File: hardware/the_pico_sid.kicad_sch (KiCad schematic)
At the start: 20 parts, among them J2 Conn_01x05, Q1 2N7002, Q2 2N7002, U1 LM324, U2 SID_6581, U3 Pico, U4 4050, U5 4050, U6 74HC245

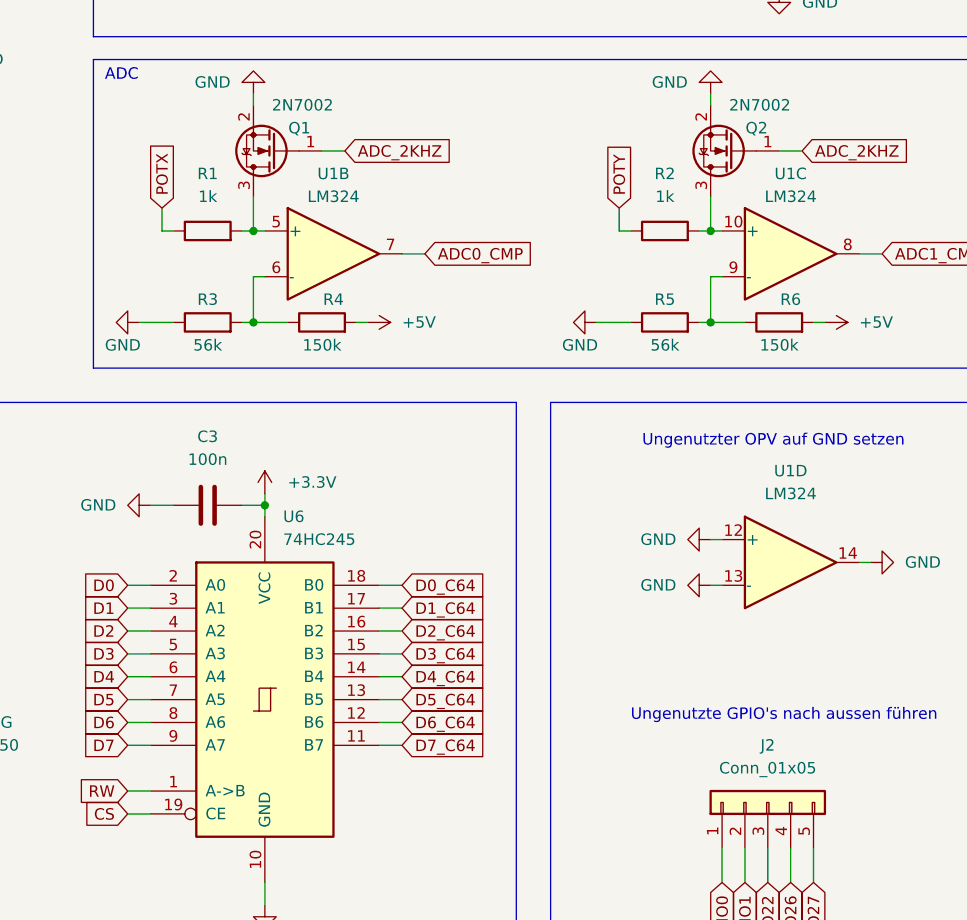
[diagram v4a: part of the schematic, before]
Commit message: change schematic: adc's inverted input voltage from 1.2V to 1.7V
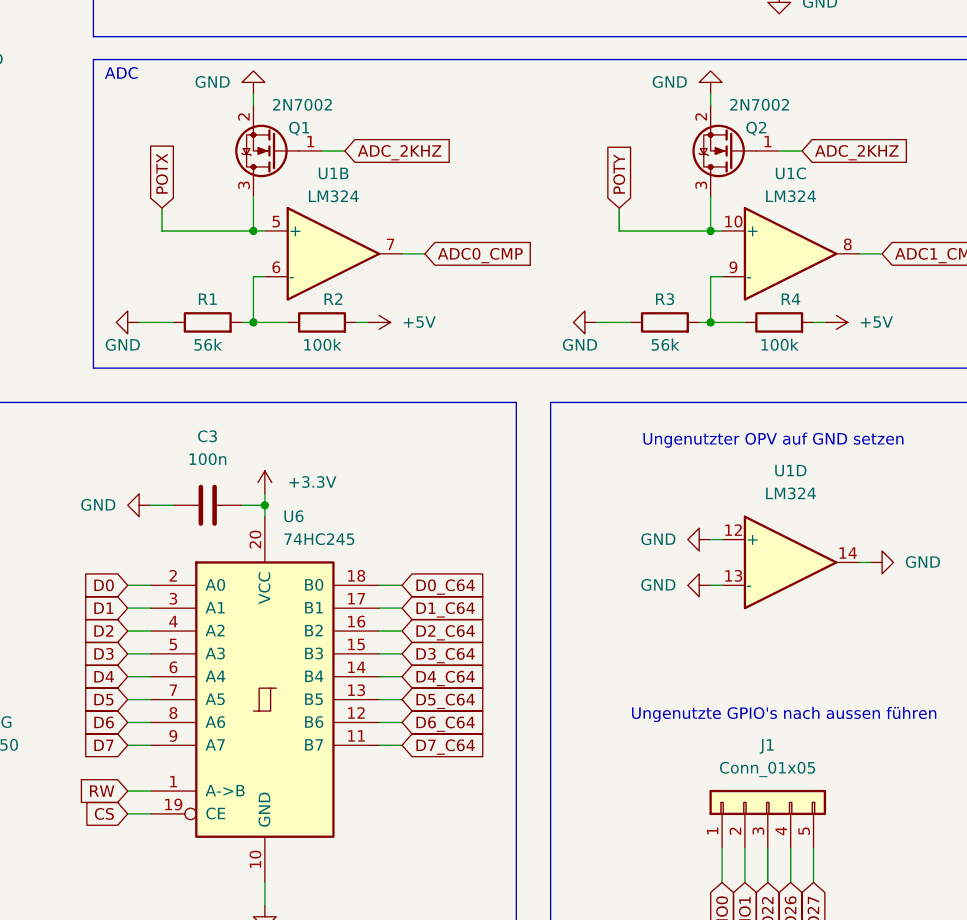
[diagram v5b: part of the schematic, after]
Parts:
- removed R1, R2: 1k, Resistor_SMD:R_0805_2012Metric_Pad1.20x1.40mm_HandSolder, symbol Device:R
- R2: renamed from R4; value 150k -> 100k
- R4: renamed from R6; value 150k -> 100k
- renumbered J2 to J1, R3 to R1, R5 to R3
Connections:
- net POTX: now also Q1.3 (D), U1.5 (+)
- net POTY: now also Q2.3 (D), U1.10 (+)
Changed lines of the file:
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@@
   (title_block
     (title "ThePicoSID")
-    (date "2023-10-09")
-    (rev "1.3")
+    (date "2024-01-25")
+    (rev "1.4")
     (company "Thorsten Kattanek")
   )
@@
     (stroke (width 0) (type default) (color 0 0 0 0))
   )
-  (wire (pts (xy 242.57 74.93) (xy 243.84 74.93))
-    (stroke (width 0) (type default) (color 0 0 0 0))
-  )
   (wire (pts (xy 207.01 121.92) (xy 209.55 121.92))
     (stroke (width 0) (type default) (color 0 0 0 0))
@@
     (stroke (width 0) (type default) (color 0 0 0 0))
   )
-  (wire (pts (xy 233.68 74.93) (xy 234.95 74.93))
+  (wire (pts (xy 233.68 74.93) (xy 243.84 74.93))
     (stroke (width 0) (type default) (color 0 0 0 0))
   )
@@
     (stroke (width 0) (type default) (color 0 0 0 0))
   )
-  (wire (pts (xy 191.77 74.93) (xy 193.04 74.93))
+  (wire (pts (xy 182.88 74.93) (xy 193.04 74.93))
     (stroke (width 0) (type default) (color 0 0 0 0))
   )
@@
   )
   (wire (pts (xy 207.01 124.46) (xy 209.55 124.46))
-    (stroke (width 0) (type default) (color 0 0 0 0))
-  )
-  (wire (pts (xy 182.88 74.93) (xy 184.15 74.93))
     (stroke (width 0) (type default) (color 0 0 0 0))
   )
@@
   (symbol (lib_id "Connector_Generic:Conn_01x05") (at 250.19 138.43 90) (unit 1)
     (in_bom yes) (on_board yes) (fields_autoplaced)
-    (property "Reference" "J2" (id 0) (at 250.19 132.08 90))
+    (property "Reference" "J1" (id 0) (at 250.19 132.08 90))
     (property "Value" "Conn_01x05" (id 1) (at 250.19 134.62 90))
     (property "Footprint" "Connector_PinHeader_2.54mm:PinHeader_1x05_P2.54mm_Vertical" (id 2) (at 250.19 138.43 0)
@@
     )
     (pin "1")
-  )
-  (symbol (lib_id "Device:R") (at 187.96 74.93 90) (unit 1)
-    (in_bom yes) (on_board yes) (fields_autoplaced)
-    (property "Reference" "R1" (id 0) (at 187.96 68.58 90))
-    (property "Value" "1k" (id 1) (at 187.96 71.12 90))
-    (property "Footprint" "Resistor_SMD:R_0805_2012Metric_Pad1.20x1.40mm_HandSolder" (id 2) (at 187.96 76.708 90)
-      (effects (font (size 1.27 1.27)) hide)
-    )
-    (property "Datasheet" "~" (id 3) (at 187.96 74.93 0)
-      (effects (font (size 1.27 1.27)) hide)
-    )
-    (pin "1")
-    (pin "2")
   )
   (symbol (lib_id "Device:C_Polarized") (at 199.39 35.56 90) (unit 1)
@@
   (symbol (lib_id "Device:R") (at 200.66 85.09 90) (unit 1)
     (in_bom yes) (on_board yes)
-    (property "Reference" "R4" (id 0) (at 201.93 82.55 90))
-    (property "Value" "150k" (id 1) (at 200.66 87.63 90))
+    (property "Reference" "R2" (id 0) (at 201.93 82.55 90))
+    (property "Value" "100k" (id 1) (at 200.66 87.63 90))
     (property "Footprint" "Resistor_SMD:R_0805_2012Metric_Pad1.20x1.40mm_HandSolder" (id 2) (at 200.66 86.868 90)
       (effects (font (size 1.27 1.27)) hide)
@@
   (symbol (lib_id "Device:R") (at 251.46 85.09 90) (unit 1)
     (in_bom yes) (on_board yes)
-    (property "Reference" "R6" (id 0) (at 252.73 82.55 90))
-    (property "Value" "150k" (id 1) (at 251.46 87.63 90))
+    (property "Reference" "R4" (id 0) (at 252.73 82.55 90))
+    (property "Value" "100k" (id 1) (at 251.46 87.63 90))
     (property "Footprint" "Resistor_SMD:R_0805_2012Metric_Pad1.20x1.40mm_HandSolder" (id 2) (at 251.46 86.868 90)
       (effects (font (size 1.27 1.27)) hide)
@@
   (symbol (lib_id "Device:R") (at 187.96 85.09 90) (unit 1)
     (in_bom yes) (on_board yes)
-    (property "Reference" "R3" (id 0) (at 187.96 82.55 90))
+    (property "Reference" "R1" (id 0) (at 187.96 82.55 90))
     (property "Value" "56k" (id 1) (at 187.96 87.63 90))
     (property "Footprint" "Resistor_SMD:R_0805_2012Metric_Pad1.20x1.40mm_HandSolder" (id 2) (at 187.96 86.868 90)
@@
     (pin "1")
   )
-  (symbol (lib_id "Device:R") (at 238.76 74.93 90) (unit 1)
-    (in_bom yes) (on_board yes) (fields_autoplaced)
-    (property "Reference" "R2" (id 0) (at 238.76 68.58 90))
-    (property "Value" "1k" (id 1) (at 238.76 71.12 90))
-    (property "Footprint" "Resistor_SMD:R_0805_2012Metric_Pad1.20x1.40mm_HandSolder" (id 2) (at 238.76 76.708 90)
-      (effects (font (size 1.27 1.27)) hide)
-    )
-    (property "Datasheet" "~" (id 3) (at 238.76 74.93 0)
-      (effects (font (size 1.27 1.27)) hide)
-    )
-    (pin "1")
-    (pin "2")
-  )
   (symbol (lib_id "Device:R") (at 238.76 85.09 90) (unit 1)
     (in_bom yes) (on_board yes)
-    (property "Reference" "R5" (id 0) (at 238.76 82.55 90))
+    (property "Reference" "R3" (id 0) (at 238.76 82.55 90))
     (property "Value" "56k" (id 1) (at 238.76 87.63 90))
     (property "Footprint" "Resistor_SMD:R_0805_2012Metric_Pad1.20x1.40mm_HandSolder" (id 2) (at 238.76 86.868 90)
@@
     )
     (path "/0b8132e4-5885-4336-9e9b-cd3d727c8b21"
-      (reference "J2") (unit 1) (value "Conn_01x05") (footprint "Connector_PinHeader_2.54mm:PinHeader_1x05_P2.54mm_Vertical")
+      (reference "J1") (unit 1) (value "Conn_01x05") (footprint "Connector_PinHeader_2.54mm:PinHeader_1x05_P2.54mm_Vertical")
     )
     (path "/e310122b-a6b6-45c4-bf28-e73538f1fd54"
@@
       (reference "Q2") (unit 1) (value "2N7002") (footprint "Package_TO_SOT_SMD:SOT-23")
     )
-    (path "/0f0eabd7-4d8a-45f6-8c35-b26564631504"
-      (reference "R1") (unit 1) (value "1k") (footprint "Resistor_SMD:R_0805_2012Metric_Pad1.20x1.40mm_HandSolder")
-    )
-    (path "/c1e4c0d2-30e7-452a-b9fa-0679cdc25434"
-      (reference "R2") (unit 1) (value "1k") (footprint "Resistor_SMD:R_0805_2012Metric_Pad1.20x1.40mm_HandSolder")
-    )
     (path "/8f635830-c076-4859-8b75-6f7277421c92"
+      (reference "R1") (unit 1) (value "56k") (footprint "Resistor_SMD:R_0805_2012Metric_Pad1.20x1.40mm_HandSolder")
+    )
+    (path "/5b03de6a-f68d-4d73-a978-3777bbbf8fb1"
+      (reference "R2") (unit 1) (value "100k") (footprint "Resistor_SMD:R_0805_2012Metric_Pad1.20x1.40mm_HandSolder")
+    )
+    (path "/c339dda8-004b-4c29-b5ab-577b17fcd28d"
       (reference "R3") (unit 1) (value "56k") (footprint "Resistor_SMD:R_0805_2012Metric_Pad1.20x1.40mm_HandSolder")
     )
-    (path "/5b03de6a-f68d-4d73-a978-3777bbbf8fb1"
-      (reference "R4") (unit 1) (value "150k") (footprint "Resistor_SMD:R_0805_2012Metric_Pad1.20x1.40mm_HandSolder")
-    )
-    (path "/c339dda8-004b-4c29-b5ab-577b17fcd28d"
-      (reference "R5") (unit 1) (value "56k") (footprint "Resistor_SMD:R_0805_2012Metric_Pad1.20x1.40mm_HandSolder")
-    )
     (path "/81649c43-29bd-46d8-b79a-e420ca2ce355"
-      (reference "R6") (unit 1) (value "150k") (footprint "Resistor_SMD:R_0805_2012Metric_Pad1.20x1.40mm_HandSolder")
+      (reference "R4") (unit 1) (value "100k") (footprint "Resistor_SMD:R_0805_2012Metric_Pad1.20x1.40mm_HandSolder")
     )
     (path "/70cd147c-d682-437f-9824-8098d9c94dc4"

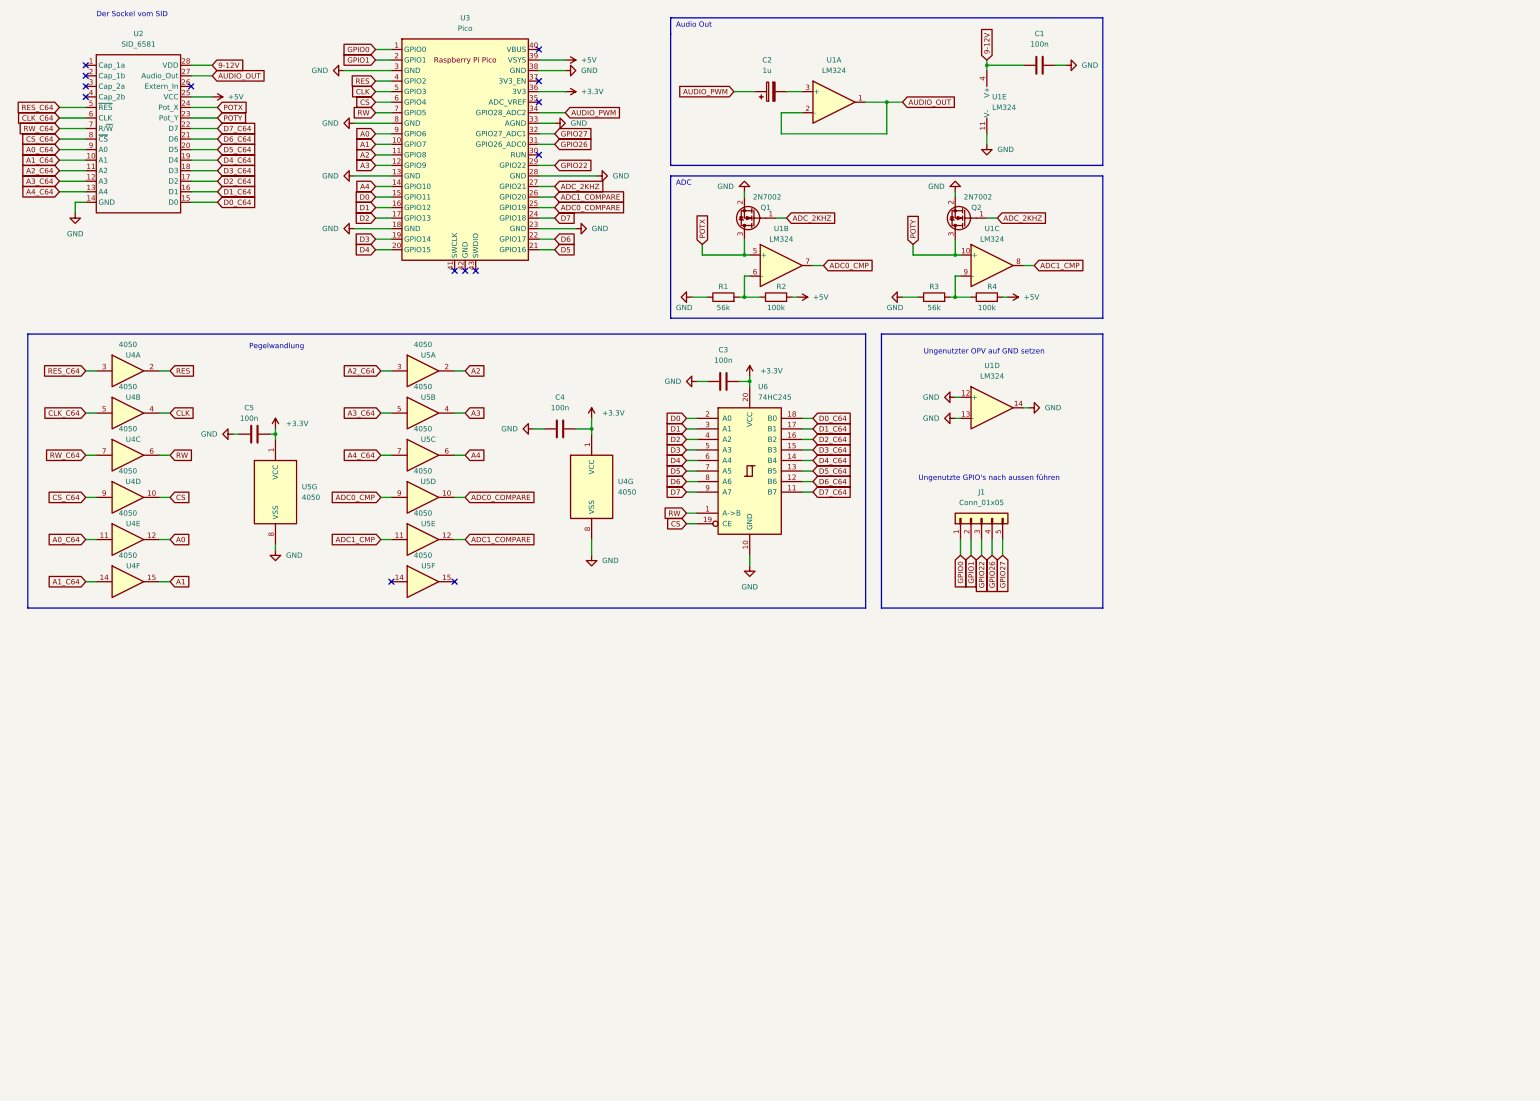
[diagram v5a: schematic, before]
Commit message: schematic: change from 4050 to resistors for level convertion
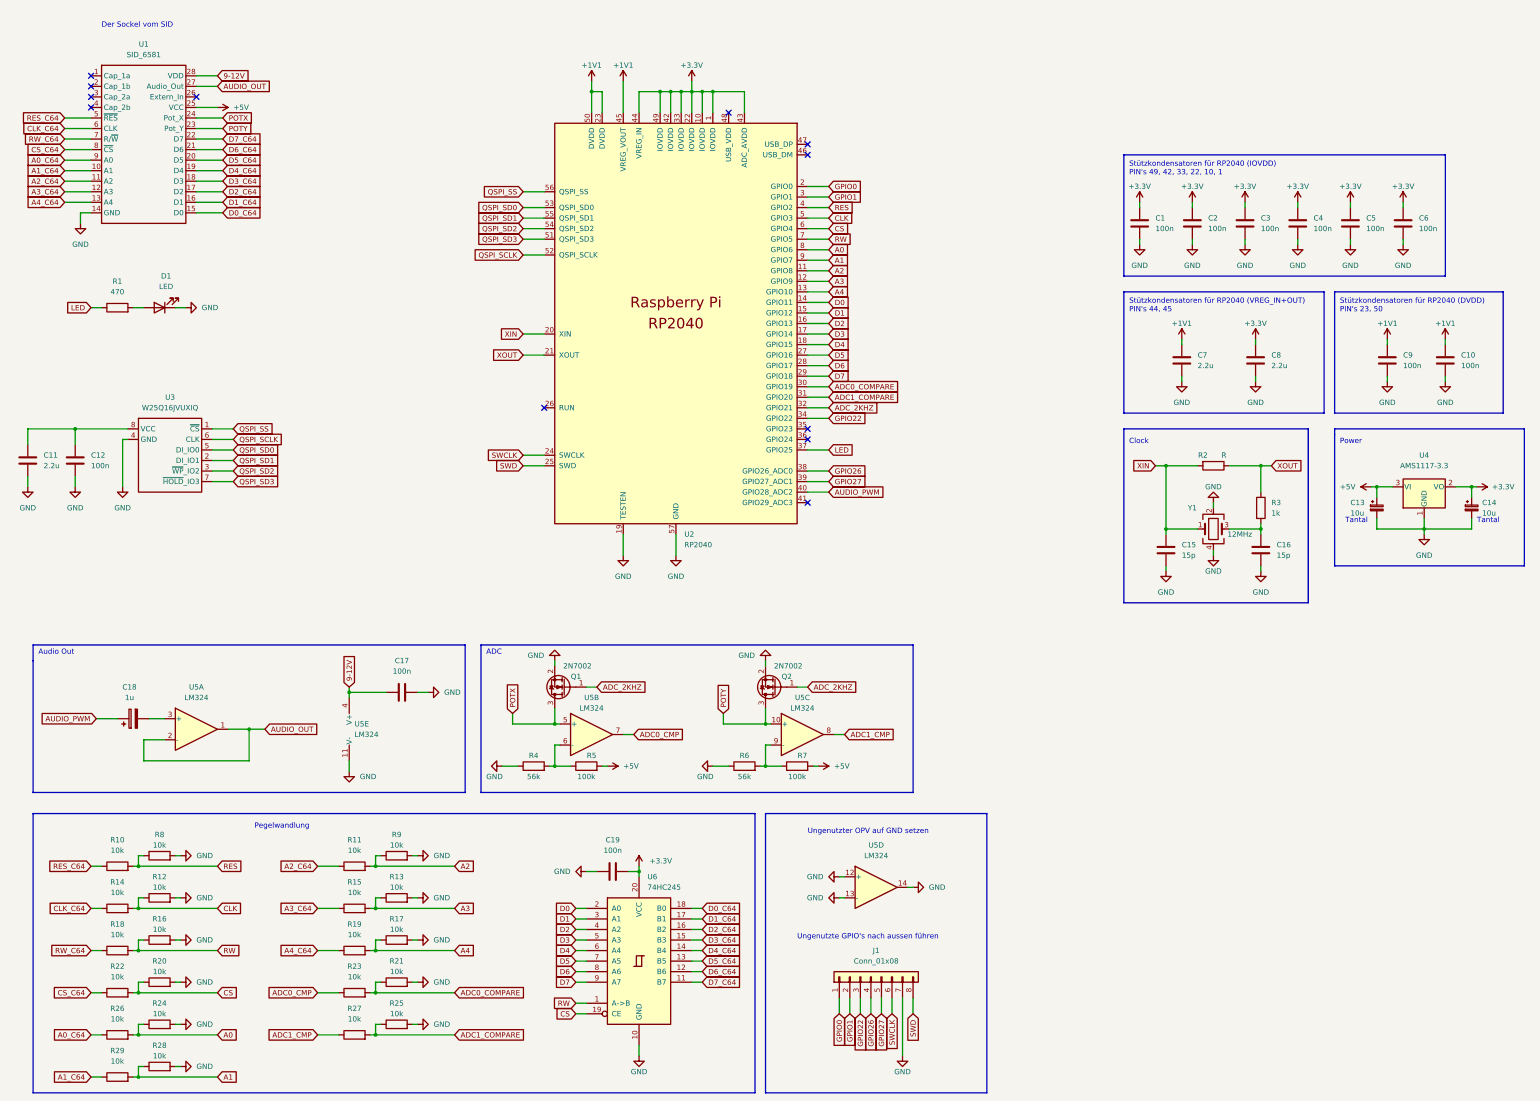
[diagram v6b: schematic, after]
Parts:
- removed J1: Conn_01x05, Connector_PinHeader_2.54mm:PinHeader_1x05_P2.54mm_Vertical, symbol Connector_Generic:Conn_01x05
- removed U3: Pico, connector_tk:RPi_Pico_SMD_TH, symbol MCU_RaspberryPi_and_Boards:Pico
- removed U4, U5: 4050, Package_SO:SOIC-16_3.9x9.9mm_P1.27mm, symbol 4xxx:4050
- added C1, C10, C12, C2, C3, C6, C9: 100n, Capacitor_SMD:C_0805_2012Metric, symbol Device:C
- added C11, C7, C8: 2.2u, Capacitor_SMD:C_0805_2012Metric, symbol Device:C
- added C13, C14: 10u, symbol Device:C_Polarized_Small
- added C15, C16: 15p, Capacitor_SMD:C_0805_2012Metric, symbol Device:C
- added D1: LED, symbol Device:LED
- added J1: Conn_01x08, symbol Connector_Generic:Conn_01x08
- added R1: 470, symbol Device:R
- added R10, R11, R12, R13, R14, R15, R16, R17, R18, R19, R20, R21, R22, R23, R24, R25, R26, R27, R28, R29, R8, R9: 10k, symbol Device:R
- added R2: R, symbol Device:R
- added R3: 1k, symbol Device:R
- added U2: RP2040, MCU_RaspberryPi_and_Boards:RP2040-QFN-56, symbol MCU_RaspberryPi_and_Boards:RP2040
- added U3: W25Q16JVUXIQ, Package_SO:SOIC-8W_5.3x5.3mm_P1.27mm, symbol ic_tk:W25Q16JVUXIQ
- added U4: AMS1117-3.3, Package_TO_SOT_SMD:SOT-223-3_TabPin2, symbol Regulator_Linear:AMS1117-3.3
- added Y1: 12MHz, symbol Device:Crystal_GND24
- C17: renamed from C1; footprint Capacitor_SMD:C_0805_2012Metric_Pad1.18x1.45mm_HandSolder -> Capacitor_SMD:C_0805_2012Metric
- C19: renamed from C3; footprint Capacitor_SMD:C_0805_2012Metric_Pad1.18x1.45mm_HandSolder -> Capacitor_SMD:C_0805_2012Metric
- C4, C5: footprint Capacitor_SMD:C_0805_2012Metric_Pad1.18x1.45mm_HandSolder -> Capacitor_SMD:C_0805_2012Metric
- R4: renamed from R1; footprint Resistor_SMD:R_0805_2012Metric_Pad1.20x1.40mm_HandSolder -> Resistor_SMD:R_0805_2012Metric
- R5: renamed from R2; footprint Resistor_SMD:R_0805_2012Metric_Pad1.20x1.40mm_HandSolder -> Resistor_SMD:R_0805_2012Metric
- R6: renamed from R3; footprint Resistor_SMD:R_0805_2012Metric_Pad1.20x1.40mm_HandSolder -> Resistor_SMD:R_0805_2012Metric
- R7: renamed from R4; footprint Resistor_SMD:R_0805_2012Metric_Pad1.20x1.40mm_HandSolder -> Resistor_SMD:R_0805_2012Metric
- renumbered C2 to C18, U2 to U1, U1 to U5
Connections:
- net +3.3V: now also C4.1, C5.1, C1.1, C14.1, C2.1, C3.1, C6.1, C8.1, U2.1 (IOVDD), U2.10 (IOVDD), U2.22 (IOVDD), U2.33 (IOVDD), U2.42 (IOVDD), U2.43 (ADC_AVDD), U2.44 (VREG_IN), U2.49 (IOVDD), U4.2 (VO); no longer C4.2, C5.2
- net +5V: now also C13.1, U4.3 (VI)
- net A0: now also R24.1, R26.2, U2.8 (GPIO6)
- net A0_C64: now also R26.1
- net A1: now also R28.1, R29.2, U2.9 (GPIO7)
- net A1_C64: now also R29.1
- net A2: now also R11.2, R9.1, U2.11 (GPIO8)
- net A2_C64: now also R11.1
- net A3: now also R13.1, R15.2, U2.12 (GPIO9)
- net A3_C64: now also R15.1
- net A4: now also R17.1, R19.2, U2.13 (GPIO10)
- net A4_C64: now also R19.1
- net ADC0_CMP: now also R23.1
- net ADC0_COMPARE: now also R21.1, R23.2, U2.30 (GPIO19)
- net ADC1_CMP: now also R27.1
- net ADC1_COMPARE: now also R25.1, R27.2, U2.31 (GPIO20)
- net ADC_2KHZ: now also U2.32 (GPIO21)
- net AUDIO_PWM: now also U2.40 (GPIO28_ADC2)
- net CLK: now also R12.1, R14.2, U2.5 (GPIO3)
- net CLK_C64: now also R14.1
- net CS: now also R20.1, R22.2, U2.6 (GPIO4)
- net CS_C64: now also R22.1
- net D0: now also U2.14 (GPIO11)
- net D1: now also U2.15 (GPIO12)
- net D2: now also U2.16 (GPIO13)
- net D3: now also U2.17 (GPIO14)
- net D4: now also U2.18 (GPIO15)
- net D5: now also U2.27 (GPIO16)
- net D6: now also U2.28 (GPIO17)
- net D7: now also U2.29 (GPIO18)
- net GND: now also C4.2, C5.2, C1.2, C10.2, C11.2, C12.2, C13.2, C14.2, C15.2, C16.2, C2.2, C3.2, C6.2, C7.2, C8.2, C9.2, D1.1 (K), J1.7 (Pin_7), R12.2, R13.2, R16.2, R17.2, R20.2, R21.2, R24.2, R25.2, R28.2, R8.2, R9.2, U2.19 (TESTEN), U2.57 (GND), U3.4 (GND), U4.1 (GND), Y1.2, Y1.4; no longer C4.1, C5.1
- net GPIO0: now also J1.1 (Pin_1), U2.2 (GPIO0)
- net GPIO1: now also J1.2 (Pin_2), U2.3 (GPIO1)
- net GPIO22: now also J1.3 (Pin_3), U2.34 (GPIO22)
- net GPIO26: now also J1.4 (Pin_4), U2.38 (GPIO26_ADC0)
- net GPIO27: now also J1.5 (Pin_5), U2.39 (GPIO27_ADC1)
- net RES: now also R10.2, R8.1, U2.4 (GPIO2)
- net RES_C64: now also R10.1
- net RW: now also R16.1, R18.2, U2.7 (GPIO5)
- net RW_C64: now also R18.1
- new net: D1.2 (A), R1.2
- new net: C16.1, R3.2, Y1.3
- new net: C11.1, C12.1, U3.8 (VCC)
- new net +1V1: C10.1, C7.1, C9.1, U2.23 (DVDD), U2.45 (VREG_VOUT), U2.50 (DVDD)
- new net LED: R1.1, U2.37 (GPIO25)
- new net QSPI_SCLK: U2.52 (QSPI_SCLK), U3.6 (CLK)
- new net QSPI_SD0: U2.53 (QSPI_SD0), U3.5 (DI_IO0)
- new net QSPI_SD1: U2.55 (QSPI_SD1), U3.2 (DI_IO1)
- new net QSPI_SD2: U2.54 (QSPI_SD2), U3.3 (~{WP}_IO2)
- new net QSPI_SD3: U2.51 (QSPI_SD3), U3.7 (~{HOLD}_IO3)
- new net QSPI_SS: U2.56 (QSPI_SS), U3.1 (~{CS})
- new net SWCLK: J1.6 (Pin_6), U2.24 (SWCLK)
- new net SWD: J1.8 (Pin_8), U2.25 (SWD)
- new net XIN: C15.1, R2.2, U2.20 (XIN), Y1.1
- new net XOUT: R2.1, R3.1, U2.21 (XOUT)
- no-connect marks 14 -> 12
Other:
- note added: "Clock"
- note added: "Power"
- note added: "Stützkondensatoren für RP2040 (DVDD) PIN's 23, 50"
- note added: "Stützkondensatoren für RP2040 (IOVDD) PIN's 49, 42, 33, 22, 10, 1"
- note added: "Stützkondensatoren für RP2040 (VREG_IN+OUT) PIN's 44, 45"
- note added: "Tantal"
- moved on the sheet: C17, C18, C19, Q1, Q2, R4, R5, R6, R7, U1, U5A, U5B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
